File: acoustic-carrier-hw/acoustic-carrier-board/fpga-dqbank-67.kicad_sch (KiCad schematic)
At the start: 0 parts

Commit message: [carrier] Added hierarchical labels
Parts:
- added C11, C12, C19, C20: 10nF, Capacitor_SMD:C_0402_1005Metric, symbol Device:C_Small
- added C13, C14, C21, C26, C27, C48, C50: 0.1uF, Capacitor_SMD:C_0402_1005Metric, symbol Device:C_Small
- added C16: 10uF, Capacitor_SMD:C_0603_1608Metric, symbol Device:C_Small
- added C45: 5pF, Capacitor_SMD:C_0603_1608Metric, symbol Device:C_Small
- added C51: 4.7uF, Capacitor_SMD:C_0402_1005Metric, symbol Device:C_Small
- added IC1: ECP5-BGA256, iw-fpga_mcu:BGA256C80P16X16_1400X1400X170, symbol iw-fpga_mcu:ECP5-BGA256
- added L2: 120@100MHz, Inductor_SMD:L_0603_1608Metric, symbol Device:L_Small
- added R4: 1k, Resistor_SMD:R_0603_1608Metric, symbol Device:R_Small
- added Y4: Crystal Oscillator, Crystal:Crystal_SMD_3225-4Pin_3.2x2.5mm, symbol Oscillator:ASCO
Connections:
- new net: C45.1, IC1.J3 (PL20C/GR_PCLK7_0), Y4.3 (OUT)
- new net: R4.2, Y4.1 (Tri-State)
- new net A0: IC1.N4 (PL38A/LDQ44)
- new net A1: IC1.N3 (PL35D)
- new net A10: IC1.K4 (PL29A/GR_PCLK6_0)
- new net A11: IC1.M2 (PL26D/PCLKC6_0)
- new net A12: IC1.M1 (PL26C/PCLKT6_0)
- new net A13: IC1.L2 (PL26B/PCLKC6_1)
- new net A14: IC1.L1 (PL26A/LDQ32/PCLKT6_1)
- new net A2: IC1.P1 (PL35A)
- new net A3: IC1.M3 (PL32D)
- new net A4: IC1.L3 (PL32C)
- new net A5: IC1.P2 (PL32B/LDQSN32)
- new net A6: IC1.N1 (PL32A/LDQS32)
- new net A7: IC1.L5 (PL29D)
- new net A8: IC1.L4 (PL29C/PL29C)
- new net A9: IC1.K5 (PL29B)
- new net BA0: IC1.R4 (PL41C)
- new net BA1: IC1.R3 (PL41B)
- new net BA2: IC1.P4 (PL41A)
- new net CAS#: IC1.T3 (PL41D)
- new net CK: IC1.N6 (PL47B)
- new net CK#: IC1.P5 (PL47D/LLC_GPLL0C_IN)
- new net CKE: IC1.P6 (PL47C/LLC_GPLL0T_IN)
- new net CS#: IC1.T4 (PL44B/LDQSN44)
- new net GND: C11.2, C12.2, C13.2, C14.2, C16.2, C19.2, C20.2, C21.2, C26.2, C27.2, C45.2, C48.2, C50.2, C51.2, Y4.2 (GND)
- new net ODT: IC1.R5 (PL44A/LDQS44)
- new net RAS#: IC1.M6 (PL47A)
- new net RESET#: IC1.N5 (PL44D)
- new net VCORE_3V3: C27.1, C48.1, C50.1, C51.1, IC1.H6 (VCCIO7_1), IC1.H7 (VCCIO7_2), R4.1, Y4.4 (VDD)
- new net VDDR3L_0.675: IC1.R1 (PL35B/VREF1_6)
- new net VDDR3L_1.35: L2.2
- new net VDDR_BANK: C11.1, C12.1, C13.1, C14.1, C16.1, IC1.J6 (VCCIO6_1), IC1.J7 (VCCIO6_2), L2.1
- new net VDRR3L_0.675: C19.1, C20.1, C21.1, C26.1
- new net WE#: IC1.M5 (PL44C)
- no-connect marks 0 -> 35
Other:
- note added: "FPGA BANK 6 (LPDDR3)"
- note added: "FPGA BANK 7"
- note added: "Probe and fixture capacitance - For the ECP5U: 5-8 pF - Max drive strength: 15 pF"

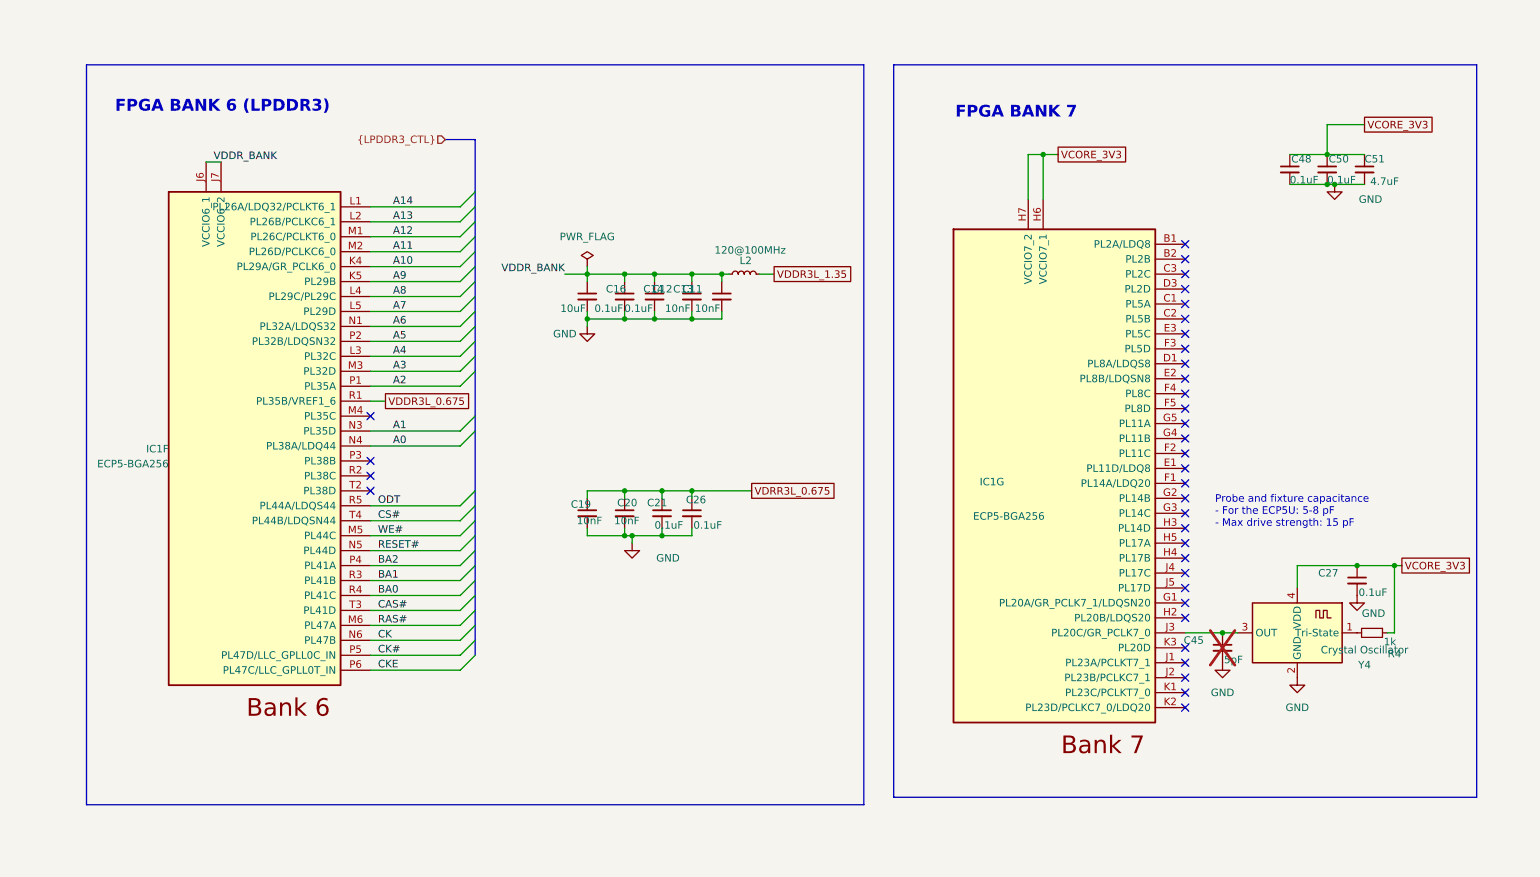
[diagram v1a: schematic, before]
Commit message: [carrier] Added decoupling caps to flash and comparators
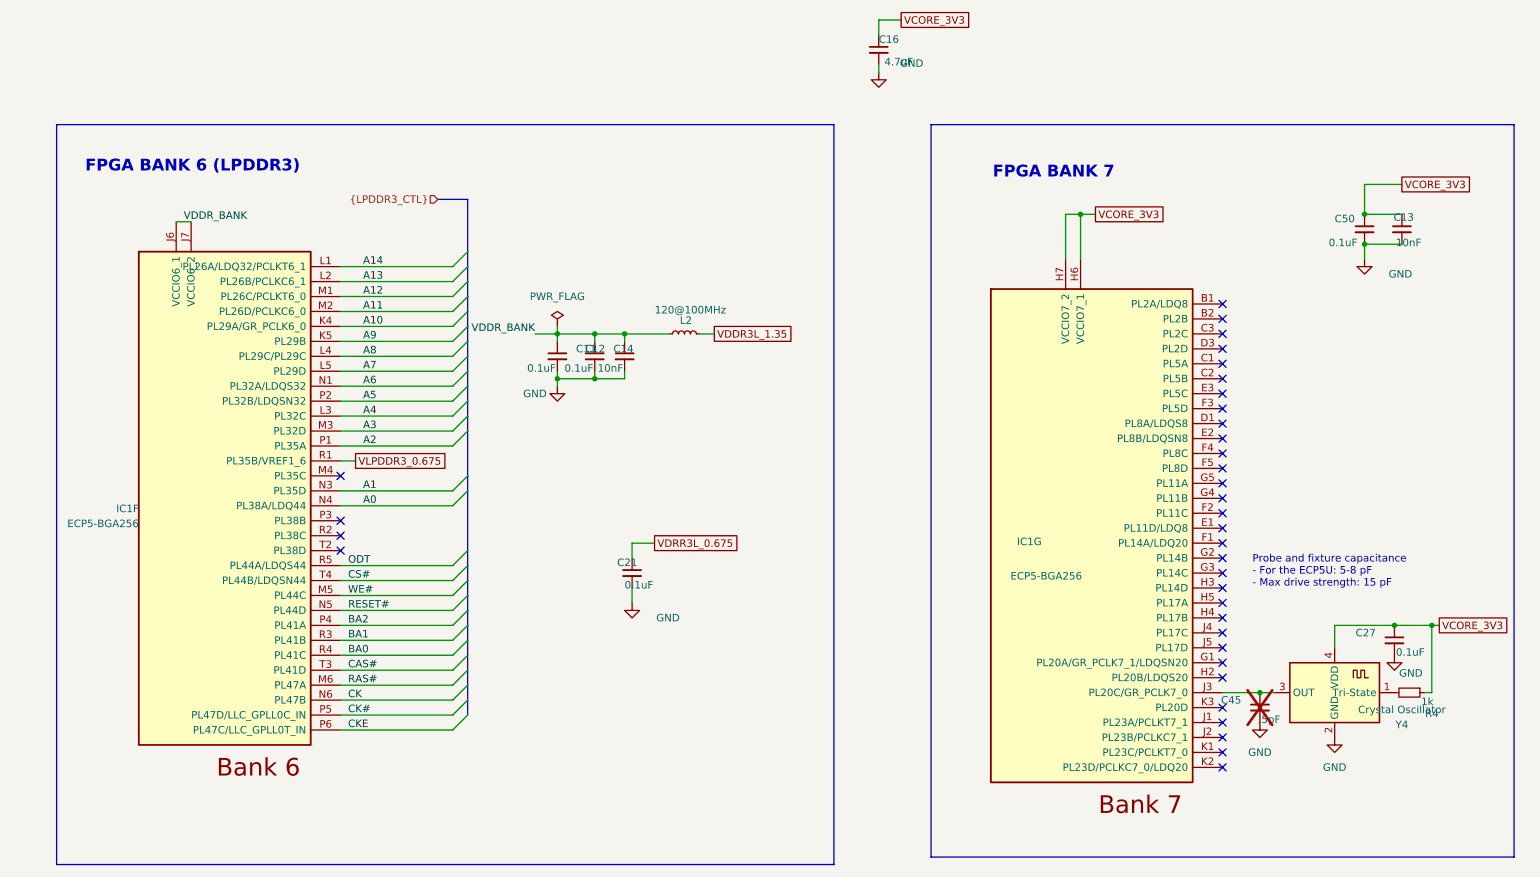
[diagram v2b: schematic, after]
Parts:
- removed C19, C20: 10nF, Capacitor_SMD:C_0402_1005Metric, symbol Device:C_Small
- removed C26, C48: 0.1uF, Capacitor_SMD:C_0402_1005Metric, symbol Device:C_Small
- removed C51: 4.7uF, Capacitor_SMD:C_0402_1005Metric, symbol Device:C_Small
- C11: value 10nF -> 0.1uF; LPN CL05B103KB5NNNC -> C307331; MPN C15195 -> CL05B104KB54PNC
- C13: value 0.1uF -> 10nF; LPN C307331 -> CL05B103KB5NNNC; MPN CL05B104KB54PNC -> C15195
- C16: value 10uF -> 4.7uF; footprint Capacitor_SMD:C_0603_1608Metric -> Capacitor_SMD:C_0402_1005Metric; LPN C19702 -> C23733; MPN CL10A106KP8NNNC -> CL05A475MP5NRNC
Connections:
- net VCORE_3V3: now also C13.1, C16.1
- net VDDR_BANK: no longer C13.1, C16.1
- net VDDR3L_0.675 renamed VLPDDR3_0.675
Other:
- moved on the sheet: C12, C14, C21, C27, C45, C50, IC1F, IC1G, L2, R4, Y4

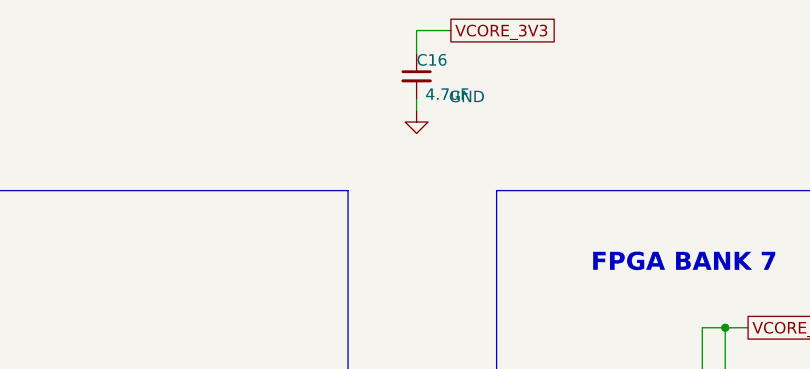
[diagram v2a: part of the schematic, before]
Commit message: [carrier] Added extra decoupling to ECP5U according to datasheet (next) perform page-wise checks, add testpoints
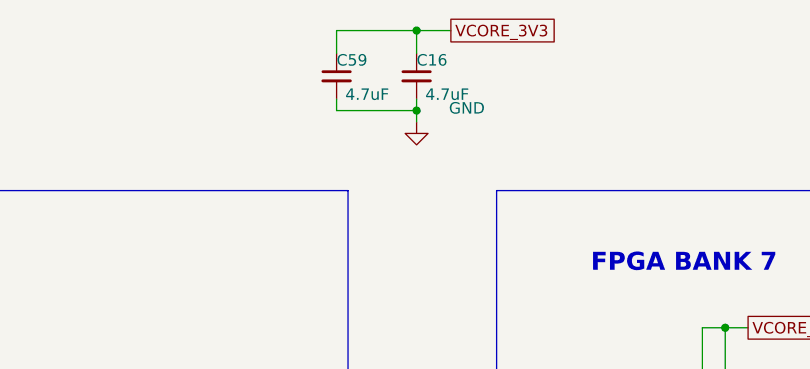
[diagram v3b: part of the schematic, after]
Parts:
- added C59: 4.7uF, Capacitor_SMD:C_0402_1005Metric, symbol Device:C_Small
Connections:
- net GND: now also C59.2
- net VCORE_3V3: now also C59.1
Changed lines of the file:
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@@
 	)
 	(junction
+		(at 162.56 15.24)
+		(diameter 0)
+		(color 0 0 0 0)
+	)
+	(junction
 		(at 250.19 118.11)
 		(diameter 0)
@@
 	)
 	(junction
+		(at 162.56 24.13)
+		(diameter 0)
+		(color 0 0 0 0)
+	)
+	(junction
 		(at 107.95 68.58)
 		(diameter 0)
@@
 	(wire
 		(pts
-			(xy 162.56 24.13) (xy 162.56 22.86)
+			(xy 162.56 25.4) (xy 162.56 24.13)
 		)
 		(stroke
@@
 		)
 	)
+	(wire
+		(pts
+			(xy 162.56 24.13) (xy 162.56 22.86)
+		)
+		(stroke
+			(width 0)
+			(type default)
+		)
+	)
 	(bus
 		(pts
@@
 	(wire
 		(pts
+			(xy 153.67 24.13) (xy 162.56 24.13)
+		)
+		(stroke
+			(width 0)
+			(type default)
+		)
+	)
+	(wire
+		(pts
 			(xy 71.12 135.89) (xy 90.17 135.89)
 		)
@@
 	(wire
 		(pts
+			(xy 153.67 24.13) (xy 153.67 22.86)
+		)
+		(stroke
+			(width 0)
+			(type default)
+		)
+	)
+	(wire
+		(pts
 			(xy 71.12 87.63) (xy 90.17 87.63)
 		)
@@
 	(wire
 		(pts
+			(xy 153.67 17.78) (xy 153.67 15.24)
+		)
+		(stroke
+			(width 0)
+			(type default)
+		)
+	)
+	(wire
+		(pts
 			(xy 71.12 57.15) (xy 90.17 57.15)
 		)
@@
 		)
 	)
+	(wire
+		(pts
+			(xy 153.67 15.24) (xy 162.56 15.24)
+		)
+		(stroke
+			(width 0)
+			(type default)
+		)
+	)
 	(bus
 		(pts
@@
 	(symbol
 		(lib_id "Device:C_Small")
+		(at 153.67 20.32 0)
+		(unit 1)
+		(exclude_from_sim no)
+		(in_bom yes)
+		(on_board yes)
+		(dnp no)
+		(property "Reference" "C59"
+			(at 153.67 18.542 0)
+			(effects
+				(font
+					(size 1.27 1.27)
+				)
+				(justify left)
+			)
+		)
+		(property "Value" "4.7uF"
+			(at 159.512 22.352 0)
+			(effects
+				(font
+					(size 1.27 1.27)
+				)
+				(justify right)
+			)
+		)
+		(property "Footprint" "Capacitor_SMD:C_0402_1005Metric"
+			(at 153.67 20.32 0)
+			(effects
+				(font
+					(size 1.27 1.27)
+				)
+				(hide yes)
+			)
+		)
+		(property "Datasheet" "https://jlcpcb.com/api/file/downloadByFileSystemAccessId/8579707315714920448"
+			(at 153.67 20.32 0)
+			(effects
+				(font
+					(size 1.27 1.27)
+				)
+				(hide yes)
+			)
+		)
+		(property "Description" "X5R, 10V"
+			(at 156.972 19.812 0)
+			(effects
+				(font
+					(size 1.27 1.27)
+				)
+				(hide yes)
+			)
+		)
+		(property "LPN" "C23733"
+			(at 153.67 20.32 0)
+			(effects
+				(font
+					(size 1.27 1.27)
+				)
+				(hide yes)
+			)
+		)
+		(property "MPN" "CL05A475MP5NRNC"
+			(at 153.67 20.32 0)
+			(effects
+				(font
+					(size 1.27 1.27)
+				)
+				(hide yes)
+			)
+		)
+		(property "Part Number" ""
+			(at 153.67 20.32 0)
+			(effects
+				(font
+					(size 1.27 1.27)
+				)
+				(hide yes)
+			)
+		)
+		(property "SN-DK" ""
+			(at 153.67 20.32 0)
+			(effects
+				(font
+					(size 1.27 1.27)
+				)
+				(hide yes)
+			)
+		)
+		(property "Sim.Pin" ""
+			(at 153.67 20.32 0)
+			(effects
+				(font
+					(size 1.27 1.27)
+				)
+				(hide yes)
+			)
+		)
+		(property "LCSC Part" ""
+			(at 153.67 20.32 0)
+			(effects
+				(font
+					(size 1.27 1.27)
+				)
+				(hide yes)
+			)
+		)
+		(pin "2"
+		)
+		(pin "1"
+		)
+		(instances
+			(project "acoustic-carrier-board"
+				(path "/25b015c9-ab13-4427-b72c-b6f348597100/9b4bf25f-717e-478b-8aa4-28cd7b267efe"
+					(reference "C59")
+					(unit 1)
+				)
+			)
+		)
+	)
+	(symbol
+		(lib_id "Device:C_Small")
 		(at 107.95 72.39 0)
 		(mirror y)
@@
 	(symbol
 		(lib_id "power:GND")
-		(at 162.56 24.13 0)
+		(at 162.56 25.4 0)
 		(unit 1)
 		(exclude_from_sim no)
@@
 		(dnp no)
 		(property "Reference" "#PWR027"
-			(at 162.56 30.48 0)
+			(at 162.56 31.75 0)
 			(effects
 				(font
@@
 		)
 		(property "Value" "GND"
-			(at 168.148 22.606 0)
+			(at 168.148 23.876 0)
 			(effects
 				(font
@@
 		)
 		(property "Footprint" ""
-			(at 162.56 24.13 0)
+			(at 162.56 25.4 0)
 			(effects
 				(font
@@
 		)
 		(property "Datasheet" ""
-			(at 162.56 24.13 0)
+			(at 162.56 25.4 0)
 			(effects
 				(font
@@
 		)
 		(property "Description" "Power symbol creates a global label with name \"GND\" , ground"
-			(at 162.56 24.13 0)
+			(at 162.56 25.4 0)
 			(effects
 				(font

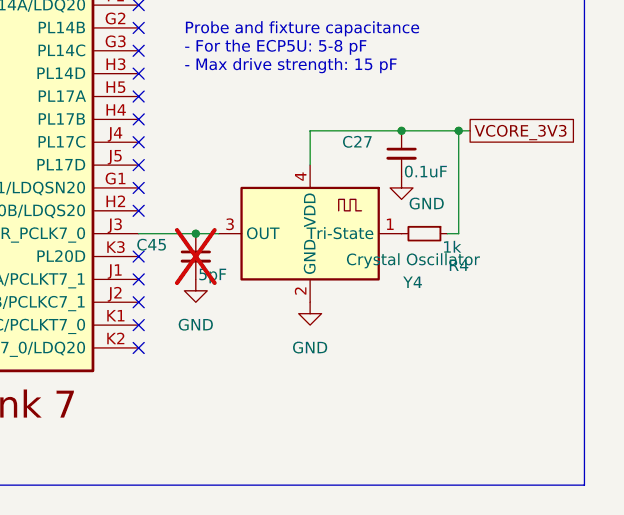
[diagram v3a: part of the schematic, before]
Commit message: [¢arrier] Finished checks, startting with layout and routing
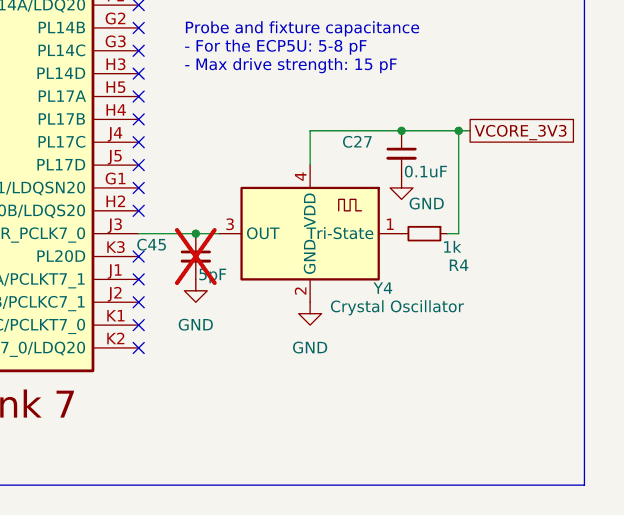
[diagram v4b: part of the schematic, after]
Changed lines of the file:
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@@
 		(dnp no)
 		(property "Reference" "Y4"
-			(at 251.46 134.9854 0)
+			(at 248.158 135.636 0)
 			(effects
 				(font
@@
 		)
 		(property "Value" "Crystal Oscillator"
-			(at 251.46 132.4454 0)
+			(at 249.682 137.668 0)
 			(effects
 				(font

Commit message: [carrier] Added testpoints
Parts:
- removed C16, C59: 4.7uF, Capacitor_SMD:C_0402_1005Metric, symbol Device:C_Small
- added C68, C69: 4.7uF, Capacitor_SMD:C_0402_1005Metric, symbol Device:C_Small
- C12, C13: LPN CL05B103KB5NNNC -> C15195; MPN C15195 -> CL05B103KB5NNNC
- R4: LPN 0603WAF1001T5E -> C21190; MPN C21190 -> 0603WAF1001T5E
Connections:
- net VLPDDR3_0.675 is gone; now on net VDRR3L_V675: IC1.R1 (PL35B/VREF1_6)
- net GND: now also C68.2, C69.2
- net VCORE_3V3: now also C69.1
- net VDDR_BANK: now also C68.1
- net A0 renamed DDR3.A0
- net A1 renamed DDR3.A1
- net A10 renamed DDR3.A10
- net A11 renamed DDR3.A11
- net A12 renamed DDR3.A12
- net A13 renamed DDR3.A13
- net A14 renamed DDR3.A14
- net A2 renamed DDR3.A2
- net A3 renamed DDR3.A3
- net A4 renamed DDR3.A4
- net A5 renamed DDR3.A5
- net A6 renamed DDR3.A6
- net A7 renamed DDR3.A7
- net A8 renamed DDR3.A8
- net A9 renamed DDR3.A9
- net BA0 renamed DDR3.BA0
- net BA1 renamed DDR3.BA1
- net BA2 renamed DDR3.BA2
- net CAS# renamed DDR3.CAS#
- net CK renamed DDR3.CK
- net CK# renamed DDR3.CK#
- net CKE renamed DDR3.CKE
- net CS# renamed DDR3.CS#
- net ODT renamed DDR3.ODT
- net RAS# renamed DDR3.RAS#
- net RESET# renamed DDR3.RESET#
- net VDDR3L_1.35 renamed VDDR3L_1V35
- net VDRR3L_0.675 renamed VDRR3L_V675
- net WE# renamed DDR3.WE#
